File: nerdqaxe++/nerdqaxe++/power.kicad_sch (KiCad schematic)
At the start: 60 parts, among them J3 Conn_01x01, J4 Conn_01x01, U3 TPS53647, U36 MCP1824T-1202E, U6 AP3211, U7 MCP1824T-0802E

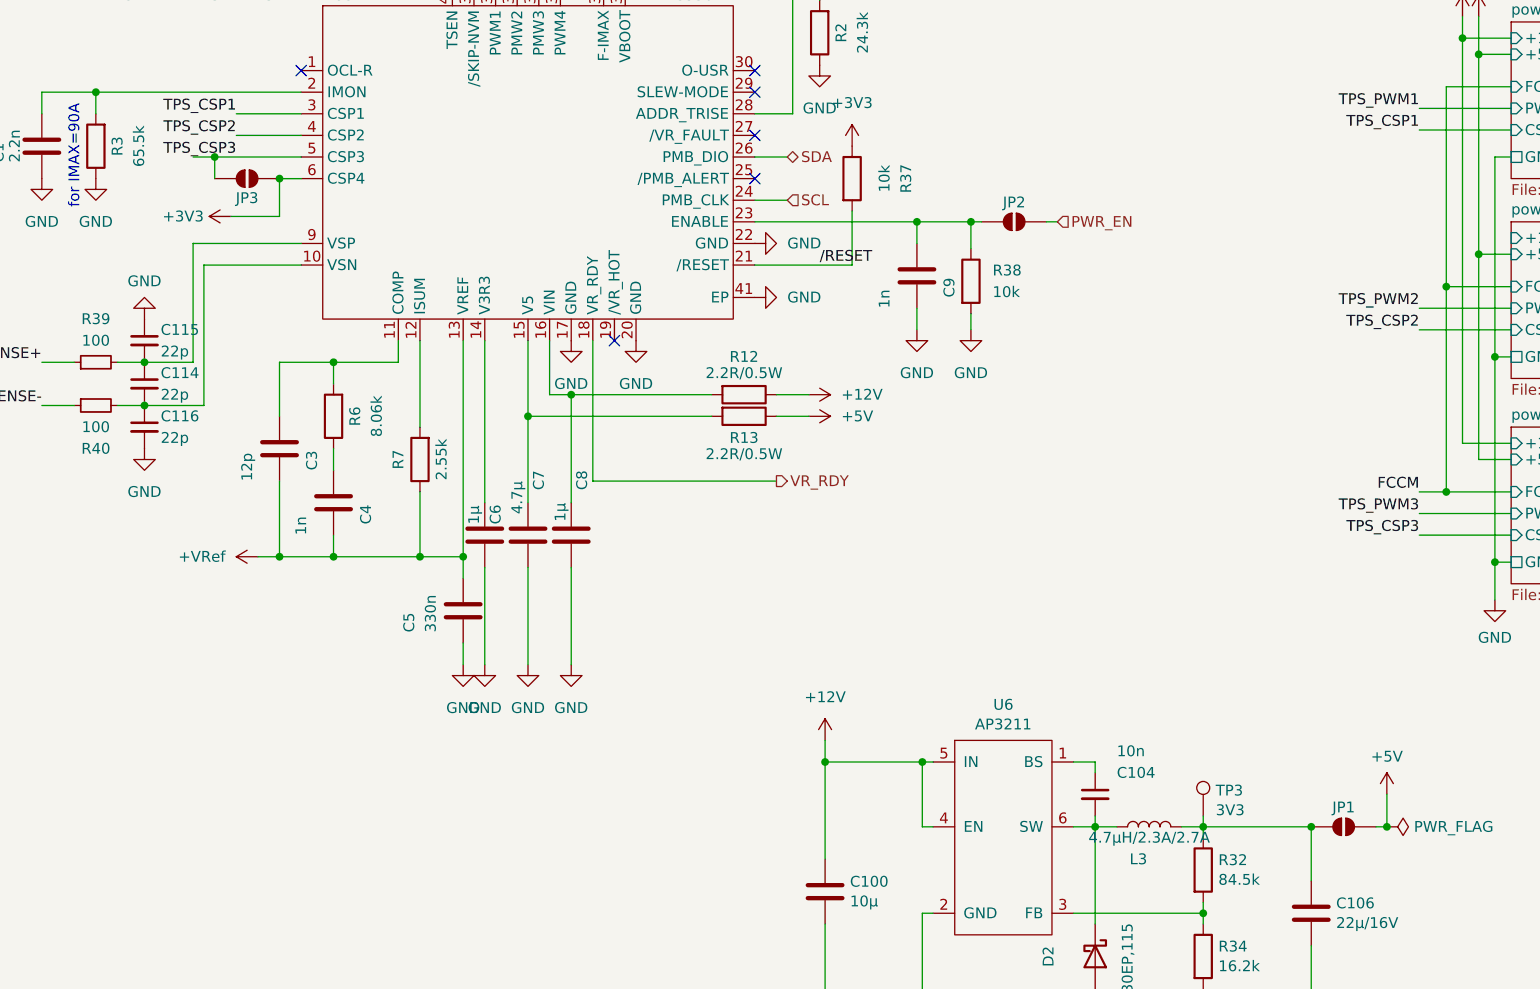
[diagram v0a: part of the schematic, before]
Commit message: removed solderjumpers on ++
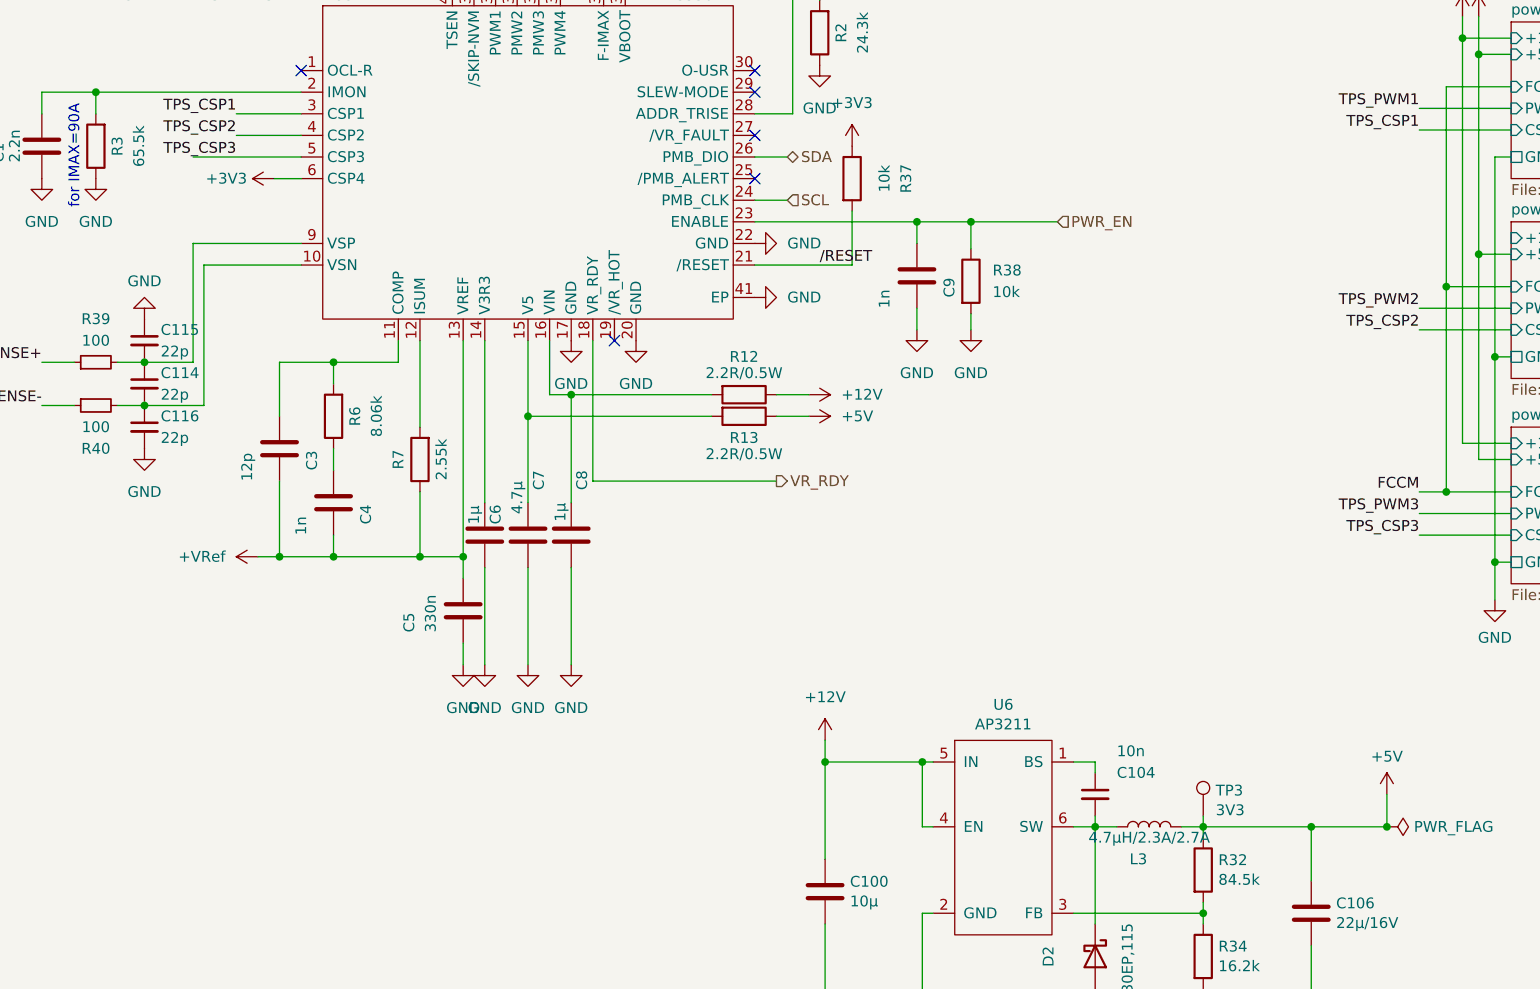
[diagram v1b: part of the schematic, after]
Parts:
- removed JP1, JP2, JP3: SolderJumper_2_Open, Jumper:SolderJumper-2_P1.3mm_Open_RoundedPad1.0x1.5mm, symbol Jumper:SolderJumper_2_Open
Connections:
- net +5V: now also C106.1, L3.2, R32.1, TP3.1
- net PWR_EN: now also C9.1, R38.1, U3.23 (ENABLE)
